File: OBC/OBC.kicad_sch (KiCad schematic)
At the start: 2 parts, among them J1 Conn_02x20_Odd_Even, U1 MPU9250

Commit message: Agrega símbolo de rpi pi zero 2w
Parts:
- removed J1: Conn_02x20_Odd_Even, symbol Connector_Generic:Conn_02x20_Odd_Even
- added J2: IDC1 (PMS-Raspi), symbol Connector_Generic:Conn_02x05_Odd_Even
- added J3: IDC2 (Raspi-TRU), symbol Connector_Generic:Conn_02x05_Odd_Even
- added U2: BMP280, symbol Cubesat:BMP280
- added U3: RASPBERRY_PI_ZERO_2_W, RASPBERRY_PI_ZERO_2_W:MODULE_RASPBERRY_PI_ZERO_2_W, symbol RASPBERRY_PI_ZERO_2_W:RASPBERRY_PI_ZERO_2_W
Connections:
- net +3.3V PMS: now reaches U1.1 (VCC)
- net +3.3V PMS: now also J2.7 (Pin_7), J2.8 (Pin_8), U2.1 (VCC)
- net GND: now reaches U1.2 (GND)
- net GND: now also J2.1 (Pin_1), J2.2 (Pin_2), J3.1 (Pin_1), J3.2 (Pin_2), U2.2 (GND), U3.6 (GND_6)
- net I2C_SCL: now reaches U1.3 (SCL)
- net I2C_SCL: now also J2.10 (Pin_10), U2.3 (SCL), U3.5 (GPIO3/SCL)
- net I2C_SDA: now reaches U1.4 (SDA)
- net I2C_SDA: now also J2.9 (Pin_9), U2.4 (SDA), U3.3 (GPIO2/SDA1)
- new net +5V PMS: J2.3 (Pin_3), J2.4 (Pin_4), J2.5 (Pin_5), J2.6 (Pin_6), U3.2 (5V_2)
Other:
- moved on the sheet: U1

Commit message: Agrega footprint de BMP280
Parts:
- U2: footprint (none) -> Charleslabs_Parts:BMP280_Module
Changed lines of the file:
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@@
 			)
 		)
-		(property "Footprint" ""
+		(property "Footprint" "Charleslabs_Parts:BMP280_Module"
 			(at 212.09 105.41 0)
 			(effects

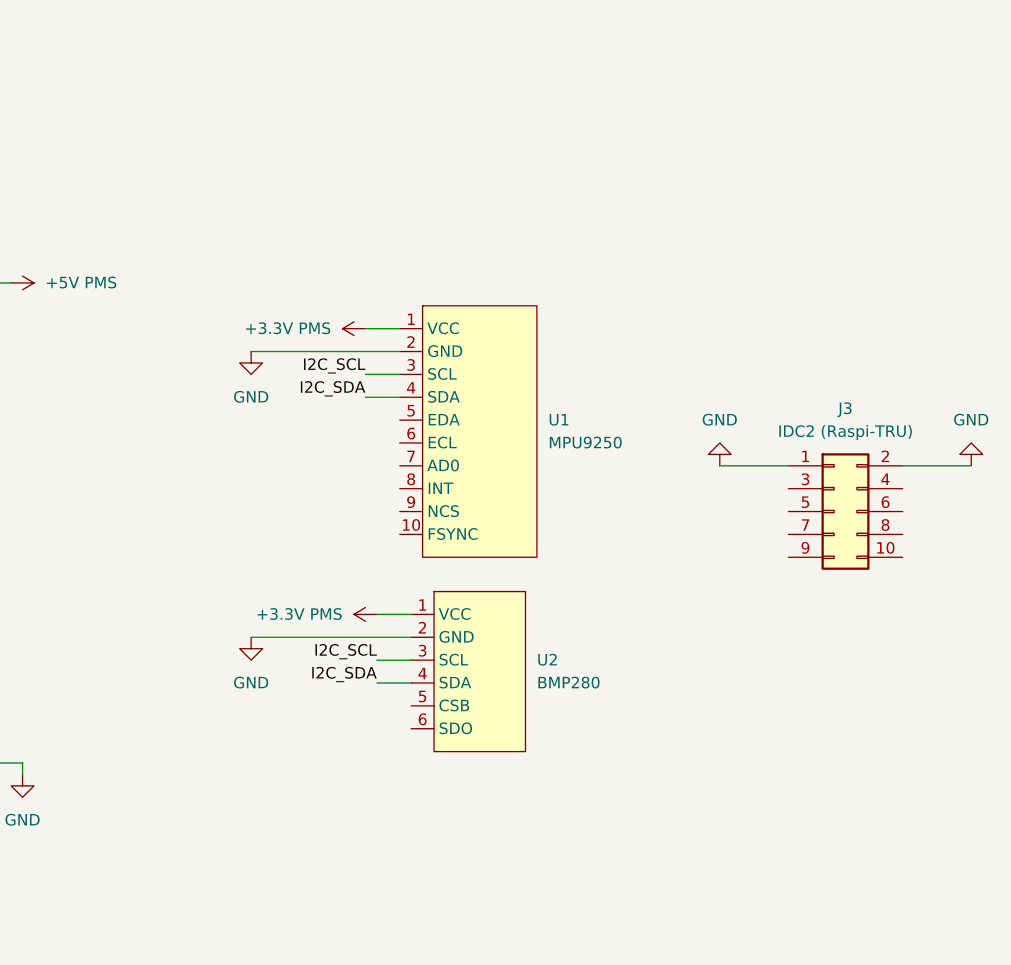
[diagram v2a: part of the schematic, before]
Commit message: Agrega módulo ADC
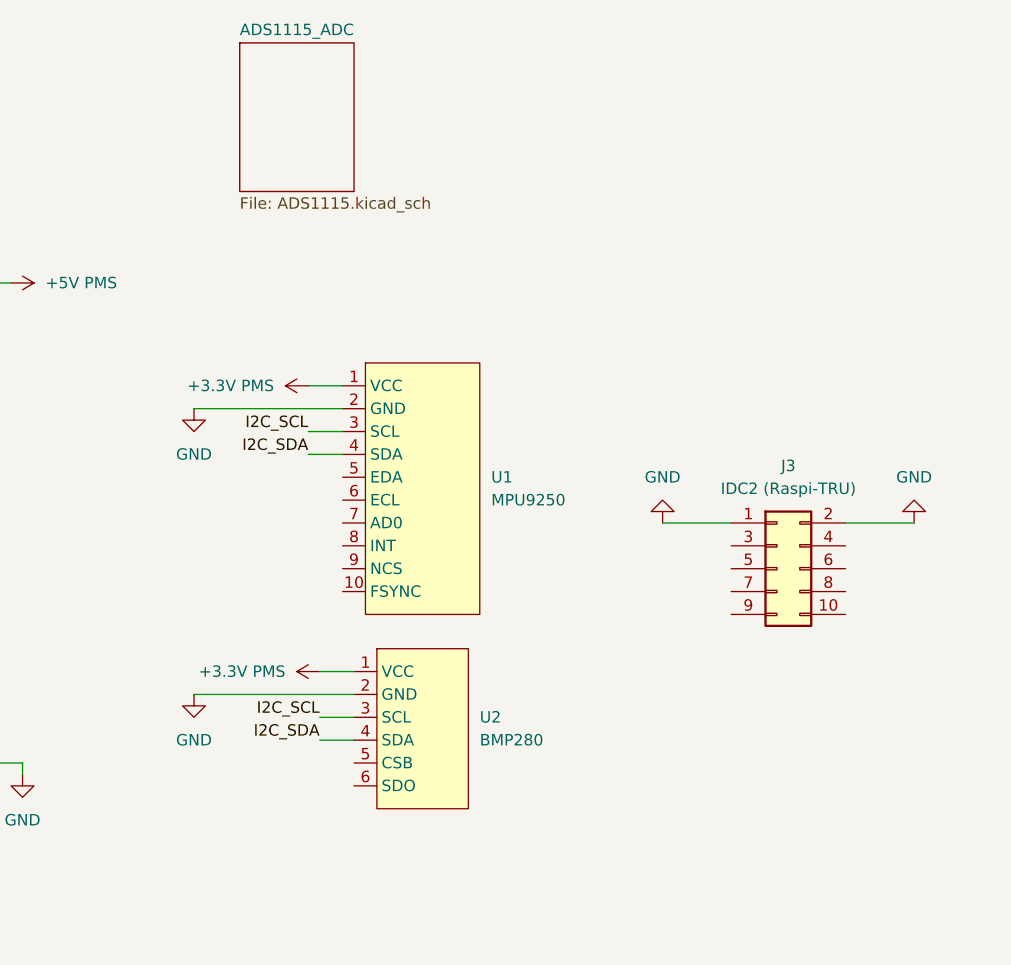
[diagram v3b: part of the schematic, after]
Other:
- added sheet ADS1115_ADC (ADS1115.kicad_sch)
- moved on the sheet: J3, U1, U2

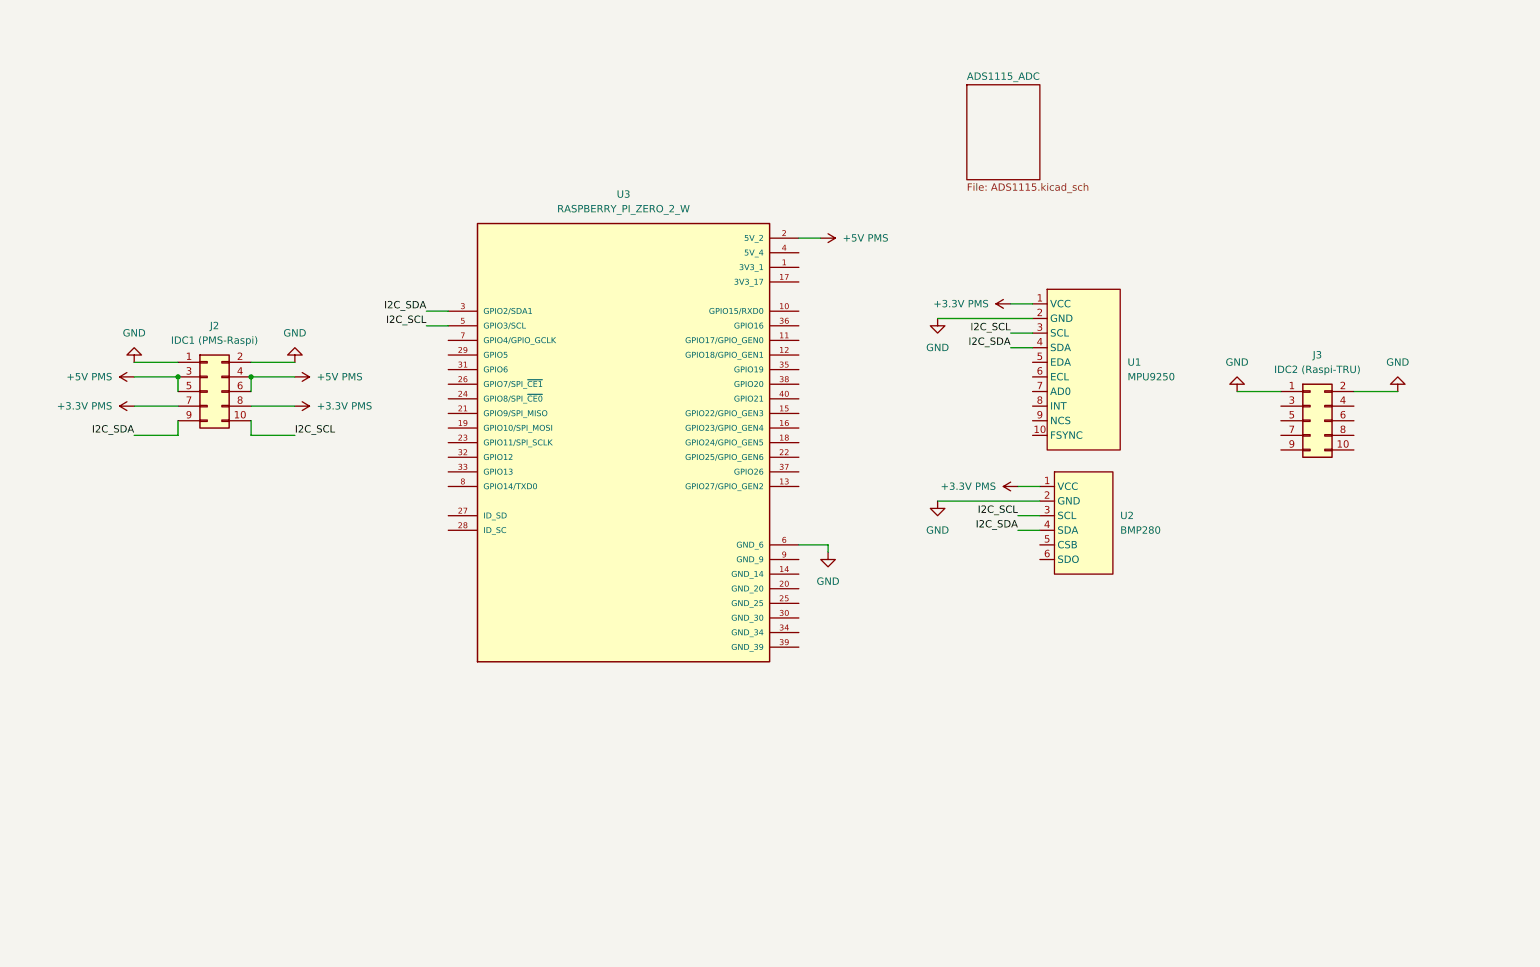
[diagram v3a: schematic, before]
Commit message: Cambia global labels por hier labels ADC
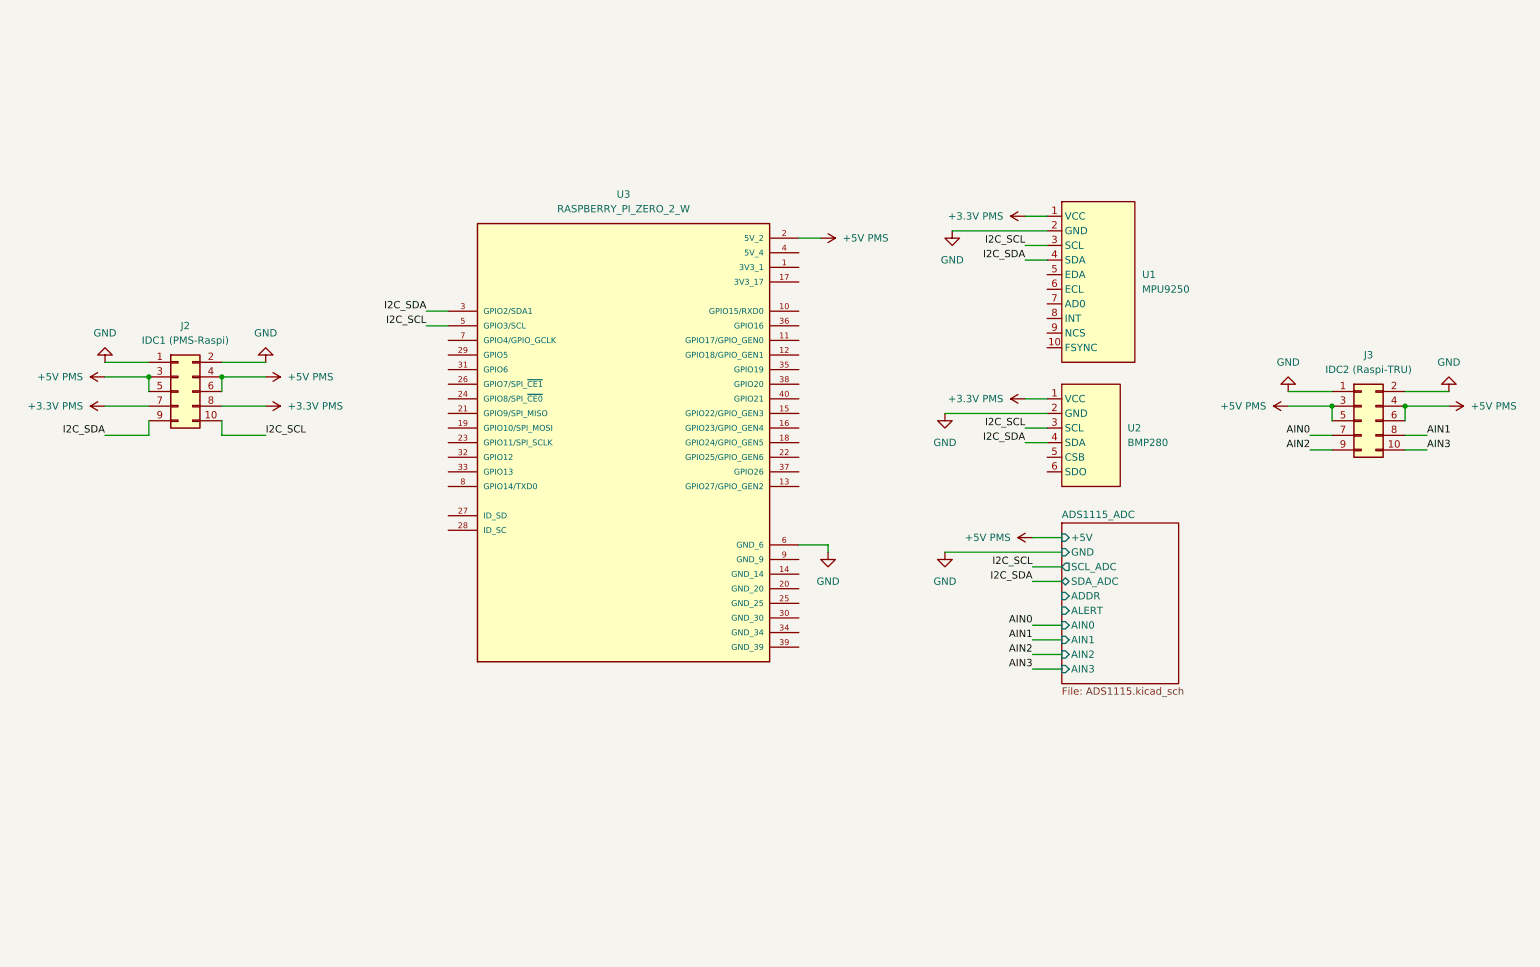
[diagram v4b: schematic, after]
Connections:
- net +5V PMS: now also J3.3 (Pin_3), J3.4 (Pin_4), J3.5 (Pin_5), J3.6 (Pin_6)
- net AIN3: now reaches J3.10 (Pin_10)
- net AIN0: now reaches J3.7 (Pin_7)
- net AIN1: now reaches J3.8 (Pin_8)
- net AIN2: now reaches J3.9 (Pin_9)
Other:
- sheet ADS1115_ADC ports: added +5V, ADDR, AIN0, AIN1, AIN2, AIN3, ALERT, GND, SCL_ADC, SDA_ADC; removed none
- moved on the sheet: J2, J3, U1, U2

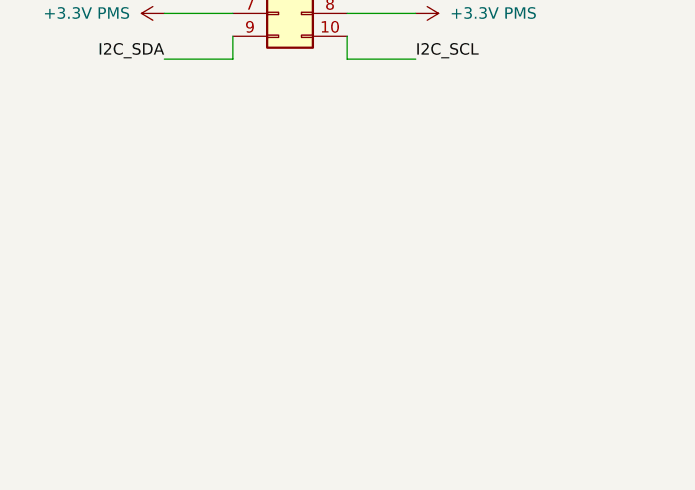
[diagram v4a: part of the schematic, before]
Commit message: Agrega resistencias pull-up para I2C
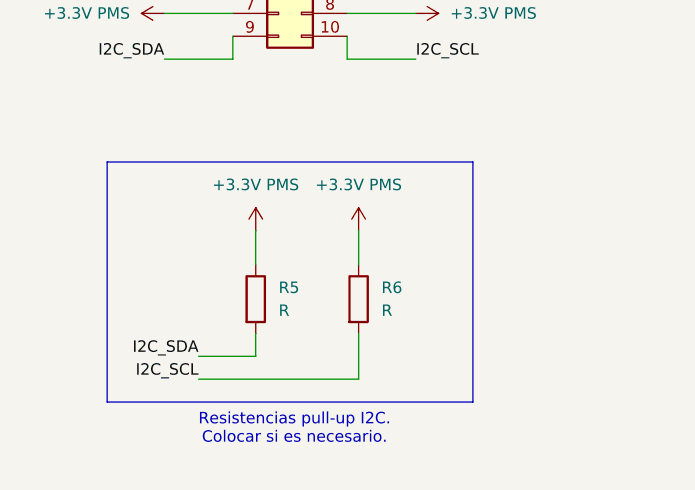
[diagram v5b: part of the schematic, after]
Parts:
- added R5, R6: R, symbol Device:R
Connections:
- net +3.3V PMS: now also R5.1, R6.1
- net I2C_SCL: now also R6.2
- net I2C_SDA: now also R5.2
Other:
- note added: "Resistencias pull-up I2C. Colocar si es necesario."

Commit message: Agrega conector para UART
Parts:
- added J4: IDC3 (Modo operación), symbol Connector_Generic:Conn_02x05_Odd_Even
- added J5: Conn_01x04, symbol Connector_Generic:Conn_01x04
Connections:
- new net RXD: J5.4 (Pin_4)
- new net TXD: J5.3 (Pin_3)
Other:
- note added: "ponemos vcc y gnd?"
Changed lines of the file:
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@@
+		)
+	)
+	(text "ponemos vcc y gnd?"
+		(exclude_from_sim no)
+		(at 255.524 142.748 0)
+		(effects
+			(font
+				(size 1.27 1.27)
+			)
 		)
 	)
@@
 	(wire
 		(pts
+			(xy 247.65 135.89) (xy 250.19 135.89)
+		)
+		(stroke
+			(width 0)
+			(type default)
+		)
+	)
+	(wire
+		(pts
 			(xy 196.85 137.16) (xy 201.93 137.16)
 		)
@@
 		(pts
 			(xy 35.56 86.36) (xy 43.18 86.36)
+		)
+		(stroke
+			(width 0)
+			(type default)
+		)
+	)
+	(wire
+		(pts
+			(xy 247.65 138.43) (xy 250.19 138.43)
 		)
 		(stroke
@@
 		)
 	)
+	(label "TXD"
+		(at 247.65 135.89 180)
+		(effects
+			(font
+				(size 1.27 1.27)
+			)
+			(justify right bottom)
+		)
+	)
 	(label "I2C_SCL"
 		(at 63.5 96.52 0)
@@
 		)
 	)
+	(label "RXD"
+		(at 247.65 138.43 180)
+		(effects
+			(font
+				(size 1.27 1.27)
+			)
+			(justify right bottom)
+		)
+	)
 	(label "I2C_SDA"
 		(at 195.58 97.79 180)
@@
 	)
 	(symbol
+		(lib_id "Connector_Generic:Conn_02x05_Odd_Even")
+		(at 254 116.84 0)
+		(unit 1)
+		(exclude_from_sim no)
+		(in_bom yes)
+		(on_board yes)
+		(dnp no)
+		(fields_autoplaced yes)
+		(property "Reference" "J4"
+			(at 255.27 105.41 0)
+			(effects
+				(font
+					(size 1.27 1.27)
+				)
+			)
+		)
+		(property "Value" "IDC3 (Modo operación)"
+			(at 255.27 107.95 0)
+			(effects
+				(font
+					(size 1.27 1.27)
+				)
+			)
+		)
+		(property "Footprint" ""
+			(at 254 116.84 0)
+			(effects
+				(font
+					(size 1.27 1.27)
+				)
+				(hide yes)
+			)
+		)
+		(property "Datasheet" "~"
+			(at 254 116.84 0)
+			(effects
+				(font
+					(size 1.27 1.27)
+				)
+				(hide yes)
+			)
+		)
+		(property "Description" "Generic connector, double row, 02x05, odd/even pin numbering scheme (row 1 odd numbers, row 2 even numbers), script generated (kicad-library-utils/schlib/autogen/connector/)"
+			(at 254 116.84 0)
+			(effects
+				(font
+					(size 1.27 1.27)
+				)
+				(hide yes)
+			)
+		)
+		(pin "2"
+		)
+		(pin "7"
+		)
+		(pin "10"
+		)
+		(pin "6"
+		)
+		(pin "5"
+		)
+		(pin "3"
+		)
+		(pin "8"
+		)
+		(pin "4"
+		)
+		(pin "9"
+		)
+		(pin "1"
+		)
+		(instances
+			(project "OBC"
+				(path "/1029d1d3-4fe2-46fb-aa7d-396827b97897"
+					(reference "J4")
+					(unit 1)
+				)
+			)
+		)
+	)
+	(symbol
 		(lib_id "power:+3.3V")
 		(at 63.5 91.44 270)
@@
 					(unit 1)
 				)
+			)
+		)
+	)
+	(symbol
+		(lib_id "Connector_Generic:Conn_01x04")
+		(at 255.27 133.35 0)
+		(unit 1)
+		(exclude_from_sim no)
+		(in_bom yes)
+		(on_board yes)
+		(dnp no)
+		(fields_autoplaced yes)
+		(property "Reference" "J5"
+			(at 257.81 133.3499 0)
+			(effects
+				(font
+					(size 1.27 1.27)
+				)
+				(justify left)
+			)
+		)
+		(property "Value" "Conn_01x04"
+			(at 257.81 135.8899 0)
+			(effects
+				(font
+					(size 1.27 1.27)
+				)
+				(justify left)
+			)
+		)
+		(property "Footprint" ""
+			(at 255.27 133.35 0)
+			(effects
+				(font
+					(size 1.27 1.27)
+				)
+				(hide yes)
+			)
+		)
+		(property "Datasheet" "~"
+			(at 255.27 133.35 0)
+			(effects
+				(font
+					(size 1.27 1.27)
+				)
+				(hide yes)
+			)
+		)
+		(property "Description" "Generic connector, single row, 01x04, script generated (kicad-library-utils/schlib/autogen/connector/)"
+			(at 255.27 133.35 0)
+			(effects
+				(font
+					(size 1.27 1.27)
+				)
+				(hide yes)
+			)
+		)
+		(pin "2"
+		)
+		(pin "4"
+		)
+		(pin "1"
+		)
+		(pin "3"
+		)
+		(instances
+			(project ""
+				(path "/1029d1d3-4fe2-46fb-aa7d-396827b97897"
+					(reference "J5")
+					(unit 1)
+				)

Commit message: Organiza sch general
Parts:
- removed J4: IDC3 (Modo operación), symbol Connector_Generic:Conn_02x05_Odd_Even
- added J6: Modo de operación, symbol Connector_Generic:Conn_02x05_Odd_Even
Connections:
- net +3.3V PMS: no longer U1.1 (VCC)
- net +5V PMS: now also U1.1 (VCC)
- net GND: now also J6.1 (Pin_1), J6.2 (Pin_2), J6.3 (Pin_3), J6.4 (Pin_4)
- net MODE_SEL0: now reaches U3.11 (GPIO17/GPIO_GEN0)
- net MODE_SEL0: now also J6.5 (Pin_5), J6.6 (Pin_6)
- net MODE_SEL2: now reaches U3.13 (GPIO27/GPIO_GEN2)
- net MODE_SEL2: now also J6.10 (Pin_10), J6.9 (Pin_9)
- net MODE_SEL1: now reaches U3.15 (GPIO22/GPIO_GEN3)
- net MODE_SEL1: now also J6.7 (Pin_7), J6.8 (Pin_8)
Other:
- note added: "Conexión con PMS"
- note added: "Conexión con TRU"
- note added: "No tiene regulador de voltaje"
- note added: "Selección modos de operación"
- note added: "Sensores de entorno"
- note added: "Tiene regulador de voltaje a 3.3V"
- moved on the sheet: J2, J3, J5, R5, R6, U1, U2, U3
